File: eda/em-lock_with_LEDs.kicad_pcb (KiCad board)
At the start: 2 copper layers, 55.9 x 55.9 mm, 75 parts, among them CON1 BARREL_JACK, P1 EXT_LED_CONN, P10 BOOT_SEL_CONN, P12 SWD_CONN, P2 RC522A, P3 RC522B, P4 BTN_OPEN, P5 BTN_CALL, P6 ESP8266_CONN, P7 LOCK_CONN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

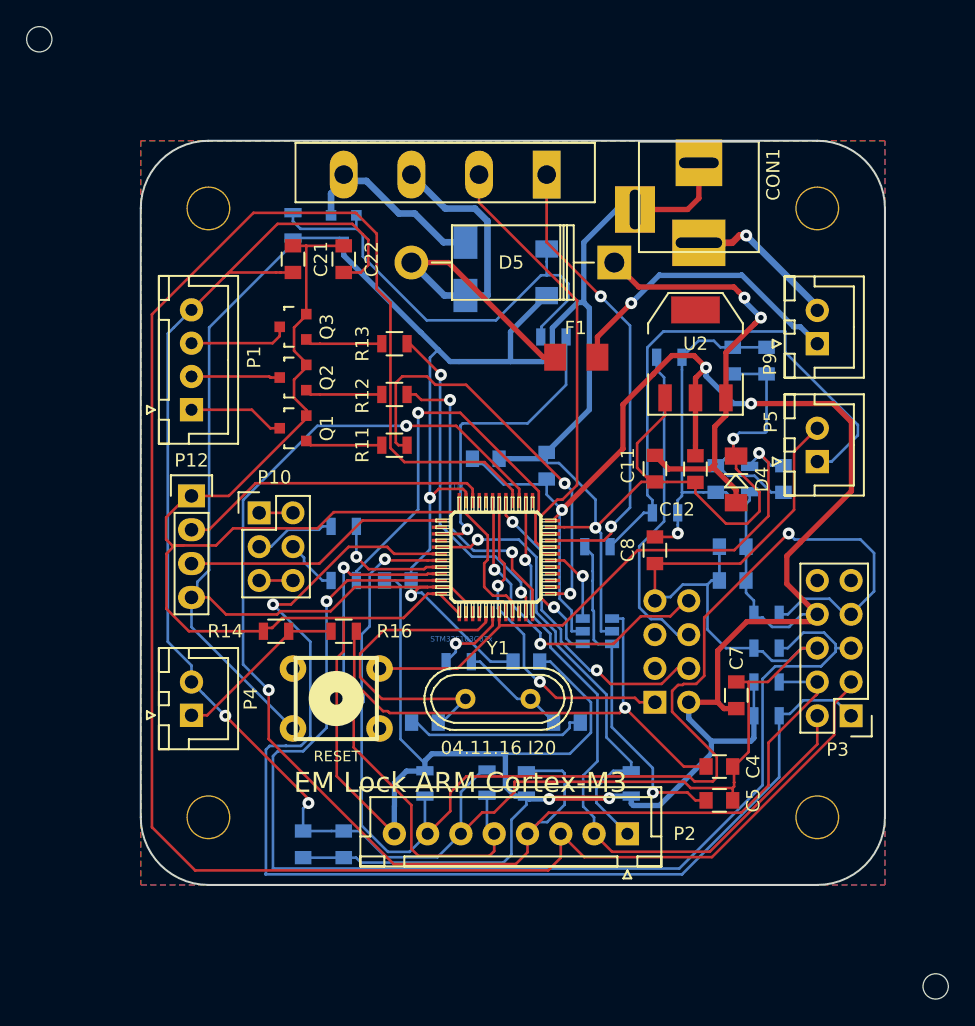
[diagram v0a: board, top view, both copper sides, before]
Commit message: refs #41563 main pcb done, todo: leds pcb multiplexor
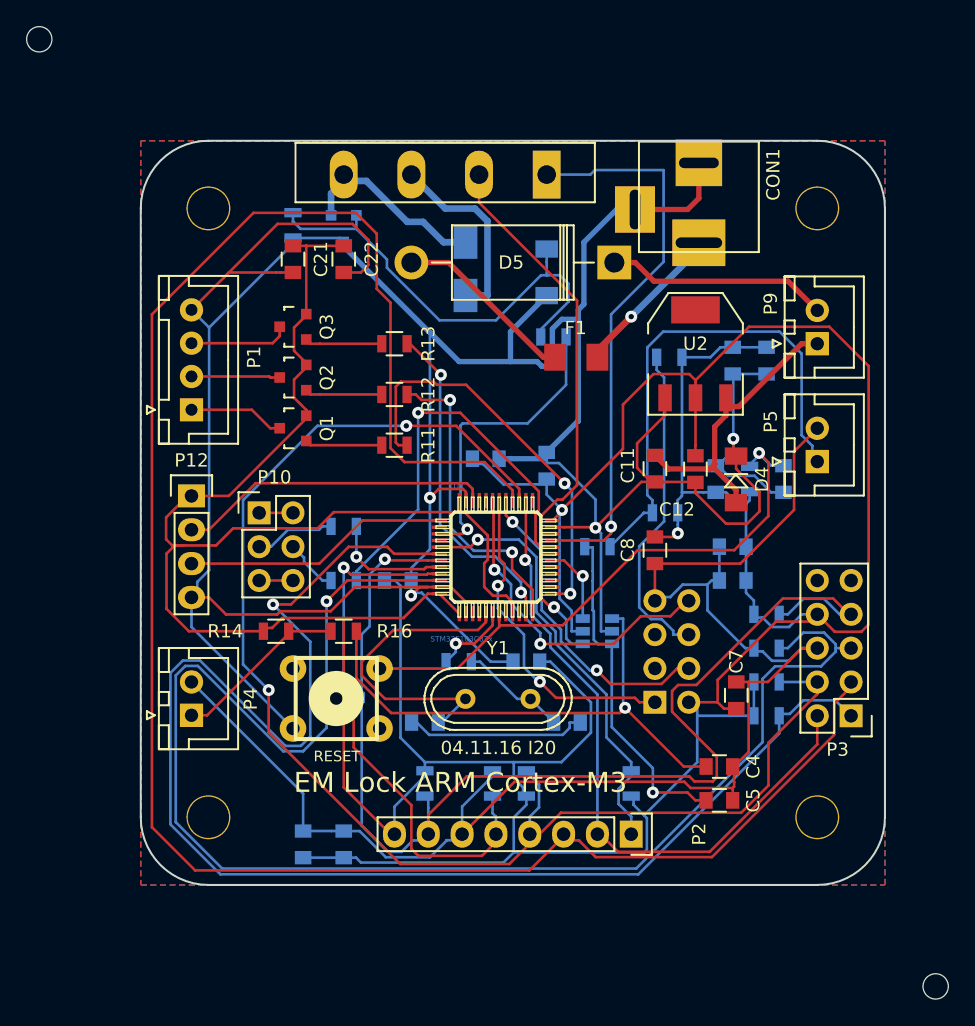
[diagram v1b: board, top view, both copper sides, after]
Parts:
- CON1: footprint I20:DC-005 -> DC-005
- P2: footprint JST_XH_B08B-XH-A_08x2.50mm_Straight -> I20:RC522_Full
- moved R7 0.42 mm to (62.0, 134.6)
- moved P2 0.29 mm to (72.4, 138.4), turned to 270 degrees
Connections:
- C21 pad 2: GNDD -> GND
- C22 pad 2: GNDD -> GND
- D5 pad 1: /stm32f103c8/LDO_IN -> Net-(D5-Pad1)
- D5 pad 2: EM_LOCK -> Net-(D5-Pad2)
- F1 pad 1: EM_LOCK -> Net-(D5-Pad2)
- F1 pad 2: Net-(F1-Pad2) -> /stm32f103c8/12V_EXT
- P1 pad 4: GNDD -> GND
- P9 pad 1: Net-(F1-Pad2) -> /stm32f103c8/LDO_IN
- P9 pad 2: /stm32f103c8/12V_EXT -> Net-(D5-Pad1)
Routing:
- net GNDD: track 171.4 -> 114.5 mm, vias 2 -> 0
- net GND: track 242.3 -> 267.8 mm
- net Net-(F1-Pad2): track 22.3 -> 0.00 mm, vias 1 -> 0
- net PB9_RC522B_IRQ: track 92.4 -> 112.0 mm
- net EM_LOCK: track 33.2 -> 14.4 mm
- net PB6_RC522B_CS: track 91.4 -> 110.1 mm
- net Net-(D5-Pad1): track 0.00 -> 16.7 mm
- net Net-(D5-Pad2): track 0.00 -> 13.7 mm
- net PB7_RC522_RST: track 101.8 -> 90.0 mm, vias 2 -> 1
- net /stm32f103c8/LDO_IN: track 33.8 -> 22.7 mm, vias 2 -> 0
- net UART_EXT_TX: track 34.7 -> 42.4 mm, vias 2 -> 1
- net VCC: track 349.0 -> 355.7 mm, vias 6 -> 2
- net PB14_SPI2_MISO: track 110.4 -> 106.2 mm
- net Net-(P5-Pad1): track 41.6 -> 38.2 mm
- net PB5_RC522A_CS: track 34.6 -> 32.6 mm
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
